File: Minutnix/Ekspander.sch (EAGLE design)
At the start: 37 parts

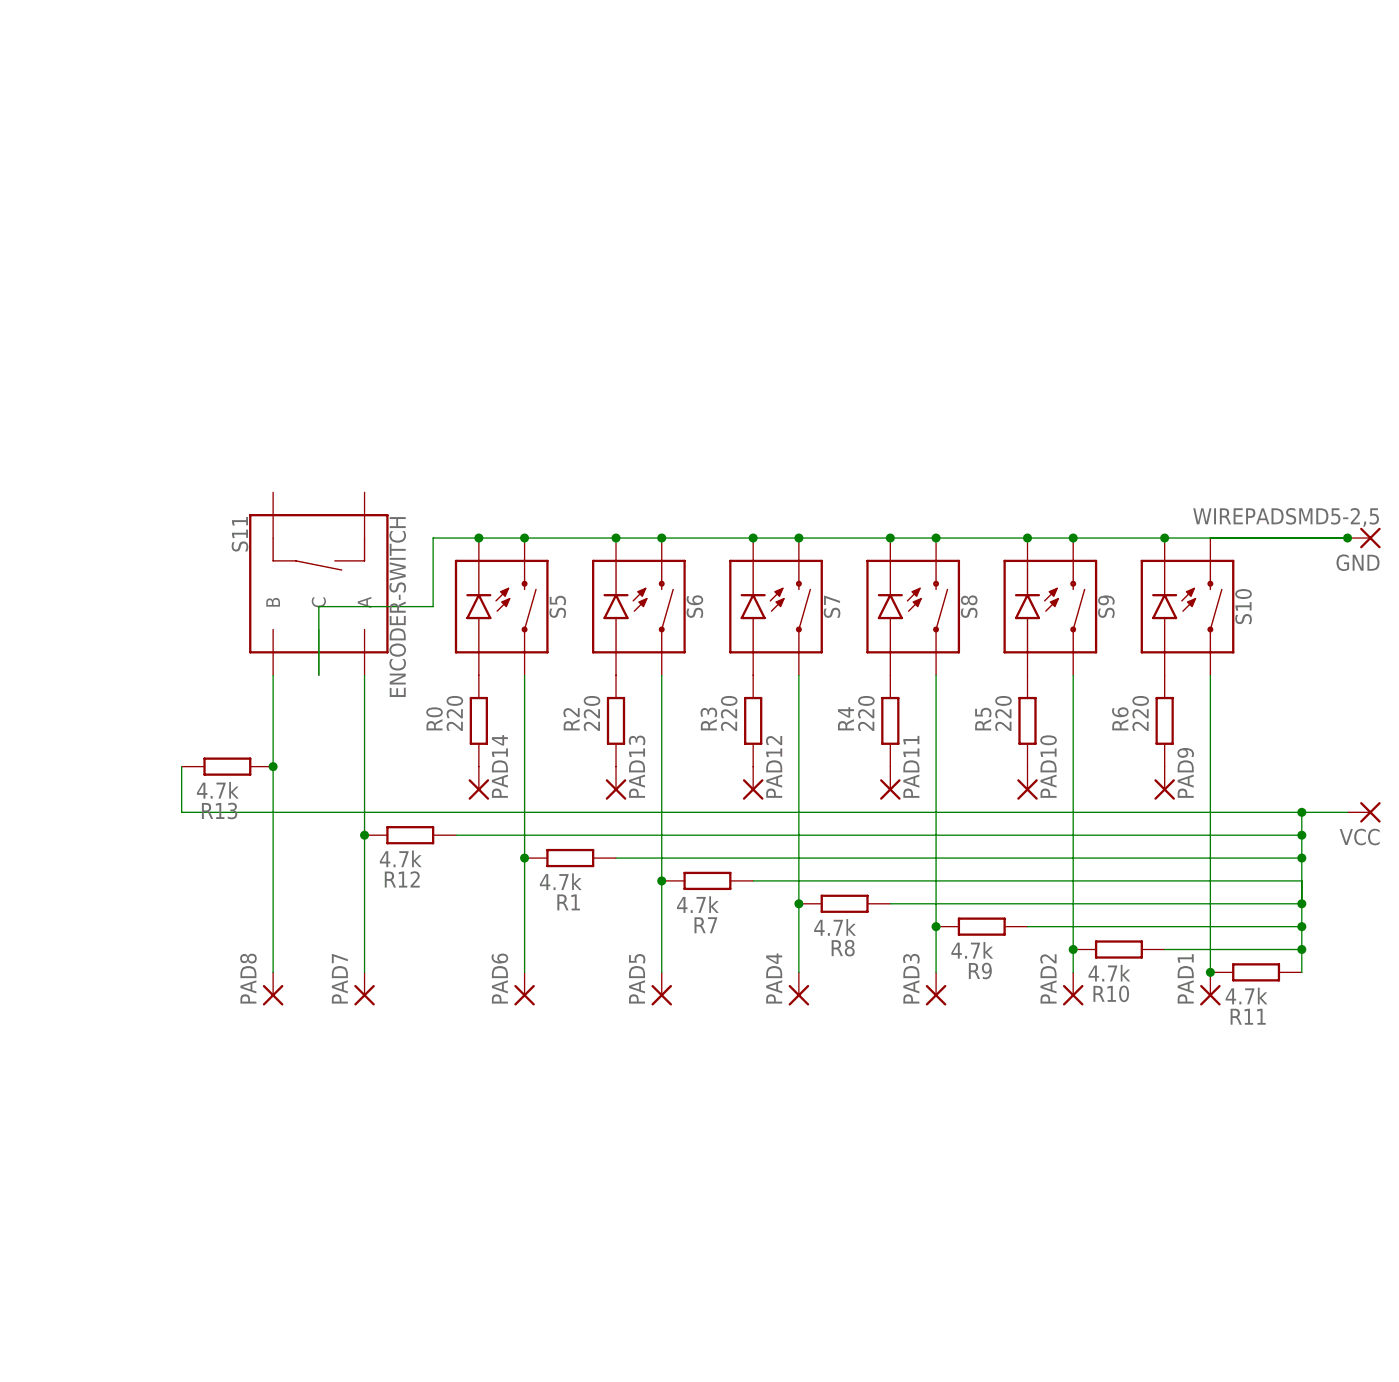
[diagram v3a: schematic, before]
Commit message: After review corrections
W programie LEDy od dwukropka sa kropkami dwoch srodkowych wyswietlaczy (wariant w ktorym segmenty wyswietlacza sa obslugiwane przez dwa osobbe rejestry przesuwny jest niekorzystny programowo)
Light sensor powinien byc podlaczony do PC0 [L1] (olewamy ADC6)
Czy na pewno podlaczenie TX ATmegi do TX FTDI ma sens? Nie powinno byc crossowania?  (oznaczenie TX dotyczy ATmegi)
Nowe podlaczenie pinow PCF na schematach (nie uzyc pinu P7)
Usunac przyciski z podswietleniem (przyciskow jest 5), 3 LEDy sygnalizujace wybrana opcje ustawien wlaczane stanem niskim na pinie ATmegi (P1 - P3)
Przycisk zwierajacy PD7 do masy na schemacie (dodaj do BOMu)
Czy jest pull-up na PC6 (RESET)?
Brakuje konektora do USBasp (wgranie bootloadera)
Niezaprogramowane piny z wyprowadzonymi padami
Podciagniecie pinu 7 ekspandera PCFa do VCC za posrednictwem rezystora 10k
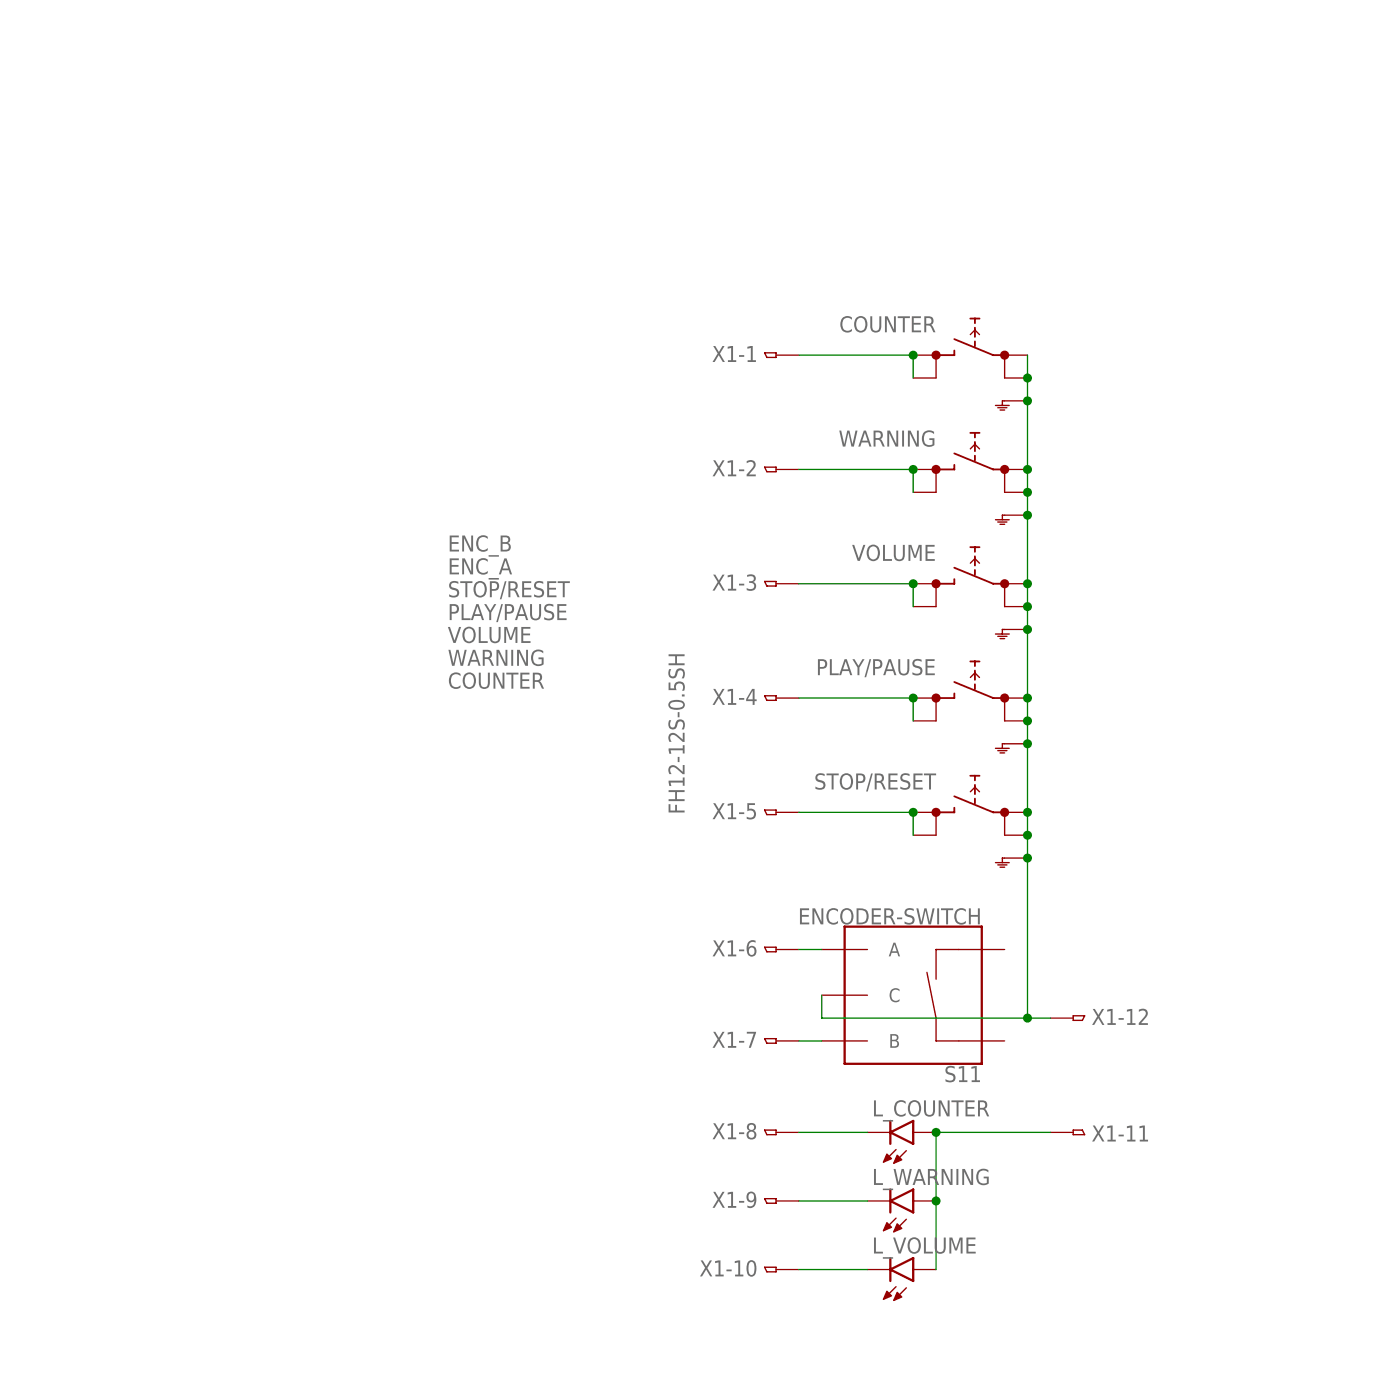
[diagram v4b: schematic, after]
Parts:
- removed GND, PAD1, PAD10, PAD11, PAD12, PAD13, PAD14, PAD2, PAD3, PAD4, PAD5, PAD6, PAD7, PAD8, PAD9, VCC: WIREPADSMD5-2,5, wirepad:WIREPADSMD5-2,5
- removed R0, R2, R3, R4, R5, R6: 220, rcl:R-EU_01005
- removed R1, R10, R11, R12, R13, R7, R8, R9: 4.7k, rcl:R-EU_01005
- removed S10, S5, S6, S7, S8, S9: MOMENTARY-SWITCH-SPST-LED-PTH-12MM, SparkFun-Switches:MOMENTARY-SWITCH-SPST-LED-PTH-12MM
- added COUNTER, PLAY/PAUSE, STOP/RESET, VOLUME, WARNING: SKHMPSE010, switch:SKHMPSE010
- added L_COUNTER, L_VOLUME, L_WARNING: (no value), led:LEDCHIPLED_0805
- added X1: FH12-12S-0.5SH, con-hirose:FH12-12S-0.5SH
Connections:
- removed net N$13: PAD1.P, R11.2, S10.1
- removed net N$14: PAD8.P, R13.1, S11.B
- removed net N$15: PAD7.P, R12.2, S11.A
- removed net N$16: PAD6.P, R1.2, S5.1
- removed net N$17: PAD5.P, R7.2, S6.1
- removed net N$18: PAD4.P, R8.2, S7.1
- removed net N$19: PAD3.P, R9.2, S8.1
- removed net N$20: PAD2.P, R10.2, S9.1
- removed net N$21: R1.1, R10.1, R11.1, R12.1, R13.2, R7.1, R8.1, R9.1, VCC.P
- removed net N$85: GND.P, S10.2, S10.C, S11.C, S5.2, S5.C, S6.2, S6.C, S7.2, S7.C, S8.2, S8.C, S9.2, S9.C
- net N$1: now also S11.A, X1-6.1; no longer R0.2, S5.A
- net N$10: now also L_COUNTER.C, X1-8.1; no longer PAD12.P, R3.1
- net N$11: now also L_WARNING.C, X1-9.1; no longer PAD13.P, R2.1
- net N$12: now also L_VOLUME.C, X1-10.1; no longer PAD14.P, R0.1
- net N$2: now also STOP/RESET.2.1, STOP/RESET.2.2, X1-5.1; no longer R2.2, S6.A
- net N$3: now also COUNTER.2.1, COUNTER.2.2, X1-1.1; no longer R3.2, S7.A
- net N$4: now also WARNING.2.1, WARNING.2.2, X1-2.1; no longer R4.2, S8.A
- net N$5: now also VOLUME.2.1, VOLUME.2.2, X1-3.1; no longer R5.2, S9.A
- net N$6: now also PLAY/PAUSE.2.1, PLAY/PAUSE.2.2, X1-4.1; no longer R6.2, S10.A
- net N$7: now also COUNTER.1.1, COUNTER.1.2, COUNTER.SH, PLAY/PAUSE.1.1, PLAY/PAUSE.1.2, PLAY/PAUSE.SH, S11.C, STOP/RESET.1.1, STOP/RESET.1.2, STOP/RESET.SH, VOLUME.1.1, VOLUME.1.2, VOLUME.SH, WARNING.1.1, WARNING.1.2, WARNING.SH, X1-12.1; no longer PAD9.P, R6.1
- net N$8: now also S11.B, X1-7.1; no longer PAD10.P, R5.1
- net N$9: now also L_COUNTER.A, L_VOLUME.A, L_WARNING.A, X1-11.1; no longer PAD11.P, R4.1
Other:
- moved on the sheet: S11

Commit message: Major board changes
Remake of interface upper board + layout
Majior corrections in mainboard - correct models, cables, connectors, ft232 and more. Also more libraries.
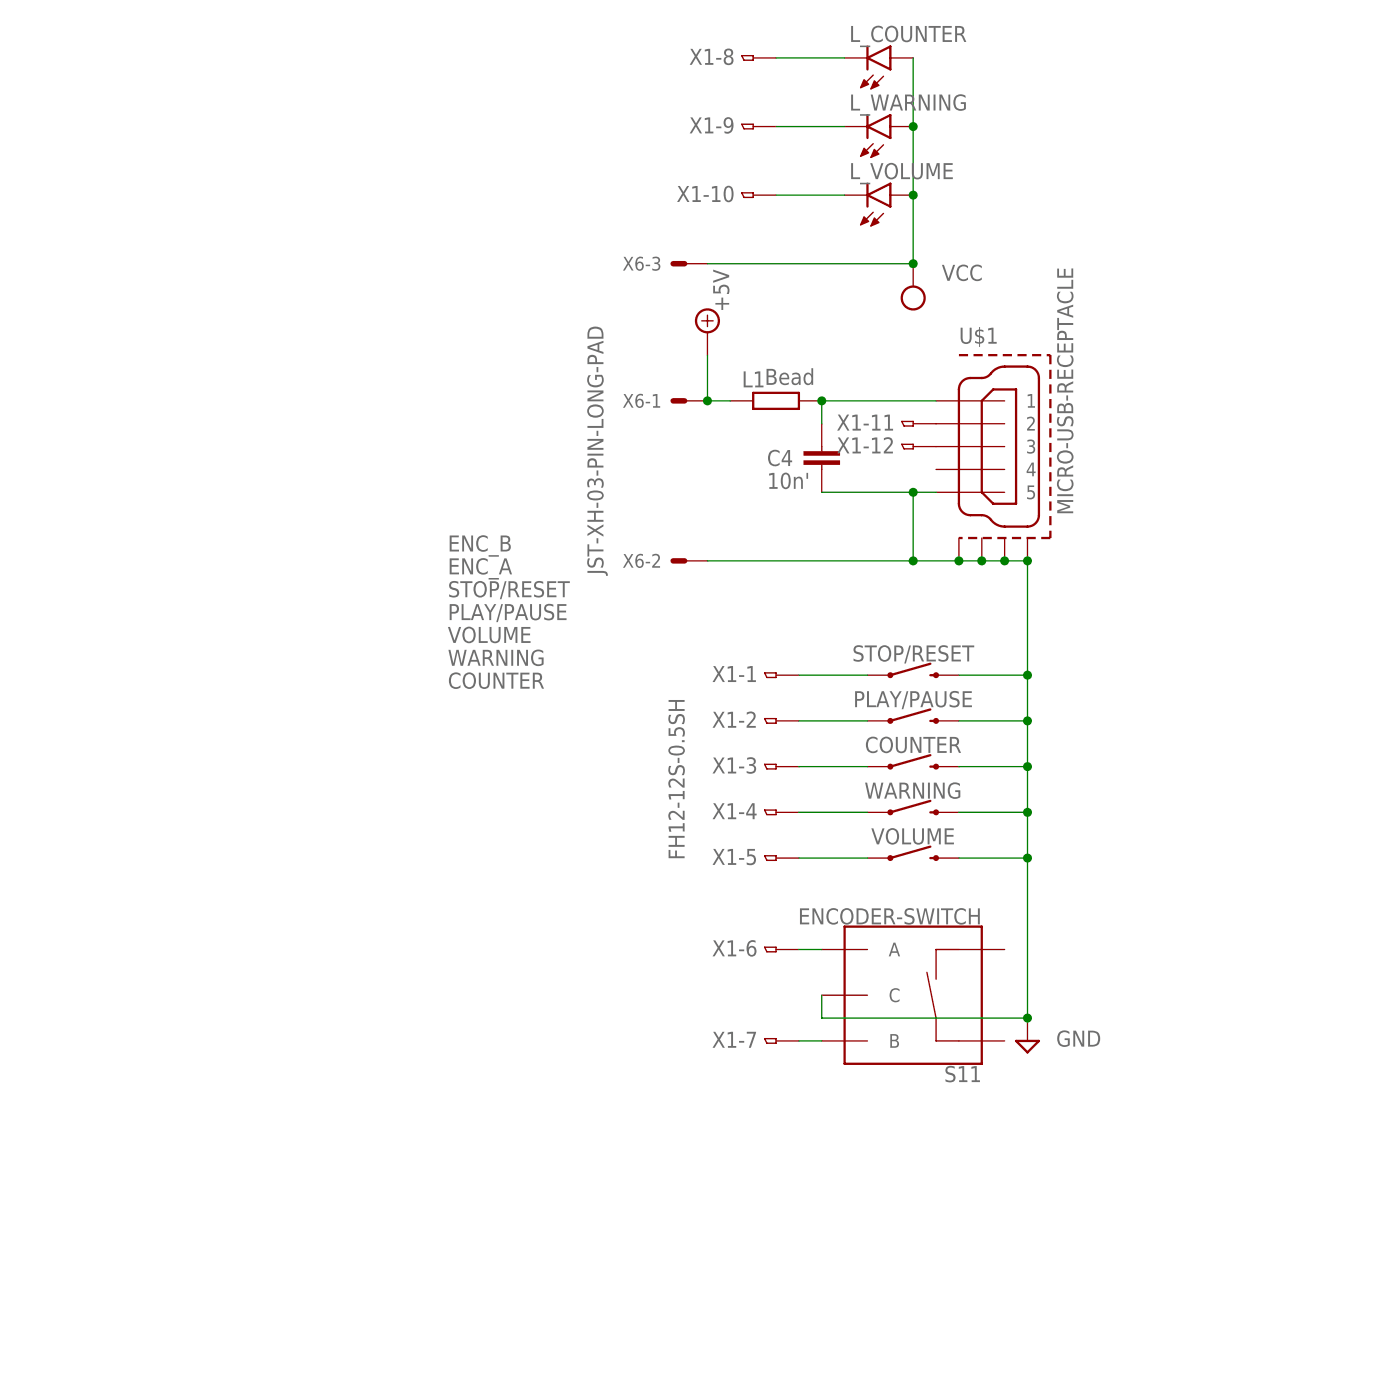
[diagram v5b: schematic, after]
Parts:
- added C4: 10n', rcl:C-EUC0603
- added L1: Bead, rcl:R-EU_R0603
- added U$1: MICRO-USB-RECEPTACLE, con-molex-usb:MICRO-USB-RECEPTACLE
- added X6: JST-XH-03-PIN-LONG-PAD, Rembrandt Electronics - JST XH Connectors v1-0:JST-XH-03-PIN-LONG-PAD
- COUNTER, PLAY/PAUSE, STOP/RESET, VOLUME, WARNING: value SKHMPSE010 -> MOMENTARY-SWITCH-SPST-PTH-12MM; device switch:SKHMPSE010 -> SparkFun-Switches:MOMENTARY-SWITCH-SPST-PTH-12MM
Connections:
- new net +5V: L1.1, X6-1.S
- new net GND: C4.2, COUNTER.2, PLAY/PAUSE.2, S11.C, STOP/RESET.2, U$1.5, U$1.GND1, U$1.GND2, U$1.GND3, U$1.GND4, VOLUME.2, WARNING.2, X6-2.S
- new net N$14: C4.1, L1.2, U$1.1
- new net VCC: L_COUNTER.A, L_VOLUME.A, L_WARNING.A, X6-3.S
- net N$2: now also STOP/RESET.1, X1-1.1; no longer STOP/RESET.2.1, STOP/RESET.2.2, X1-5.1
- net N$3: now also PLAY/PAUSE.1, X1-2.1; no longer COUNTER.2.1, COUNTER.2.2, X1-1.1
- net N$4: now also COUNTER.1, X1-3.1; no longer WARNING.2.1, WARNING.2.2, X1-2.1
- net N$5: now also WARNING.1, X1-4.1; no longer VOLUME.2.1, VOLUME.2.2, X1-3.1
- net N$6: now also VOLUME.1, X1-5.1; no longer PLAY/PAUSE.2.1, PLAY/PAUSE.2.2, X1-4.1
- net N$7: now also U$1.2, X1-11.1; no longer COUNTER.1.1, COUNTER.1.2, COUNTER.SH, PLAY/PAUSE.1.1, PLAY/PAUSE.1.2, PLAY/PAUSE.SH, S11.C, STOP/RESET.1.1, STOP/RESET.1.2, STOP/RESET.SH, VOLUME.1.1, VOLUME.1.2, VOLUME.SH, WARNING.1.1, WARNING.1.2, WARNING.SH, X1-12.1
- net N$9: now also U$1.3, X1-12.1; no longer L_COUNTER.A, L_VOLUME.A, L_WARNING.A, X1-11.1
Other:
- moved on the sheet: L_COUNTER, L_VOLUME, L_WARNING, X1-1, X1-10, X1-11, X1-12, X1-2, X1-3, X1-4, X1-5, X1-8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
